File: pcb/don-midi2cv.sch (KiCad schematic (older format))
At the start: 17 parts

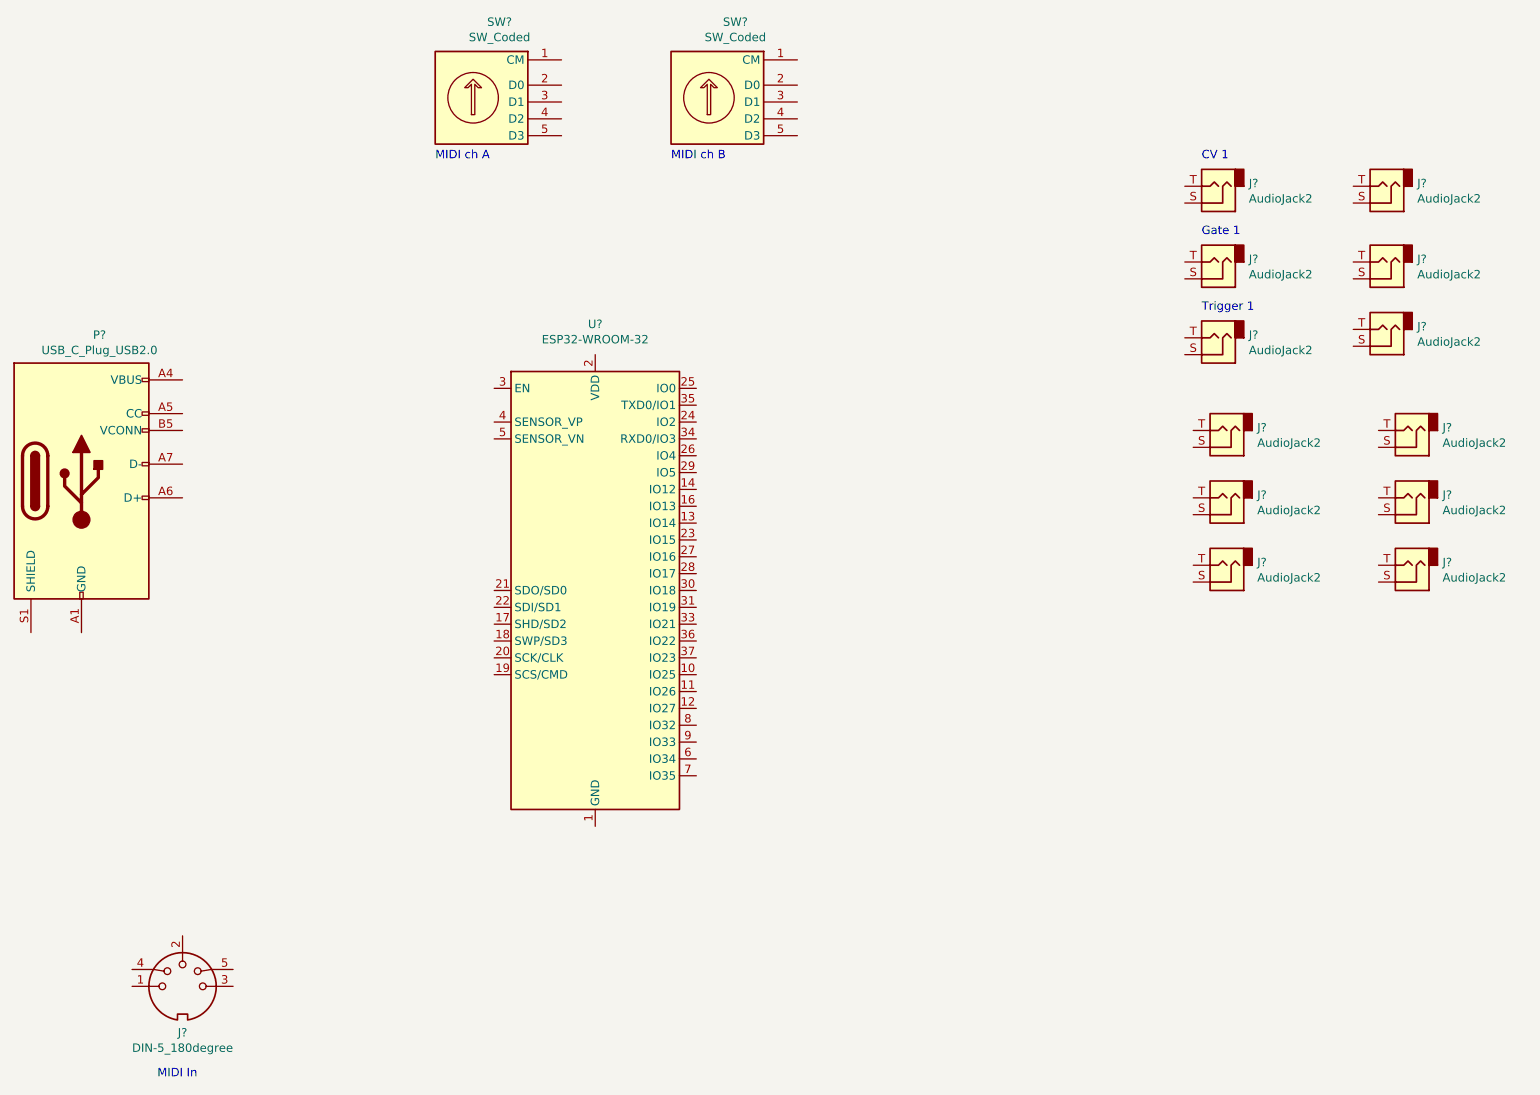
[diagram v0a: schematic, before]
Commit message: replace esp32 with stm32f103
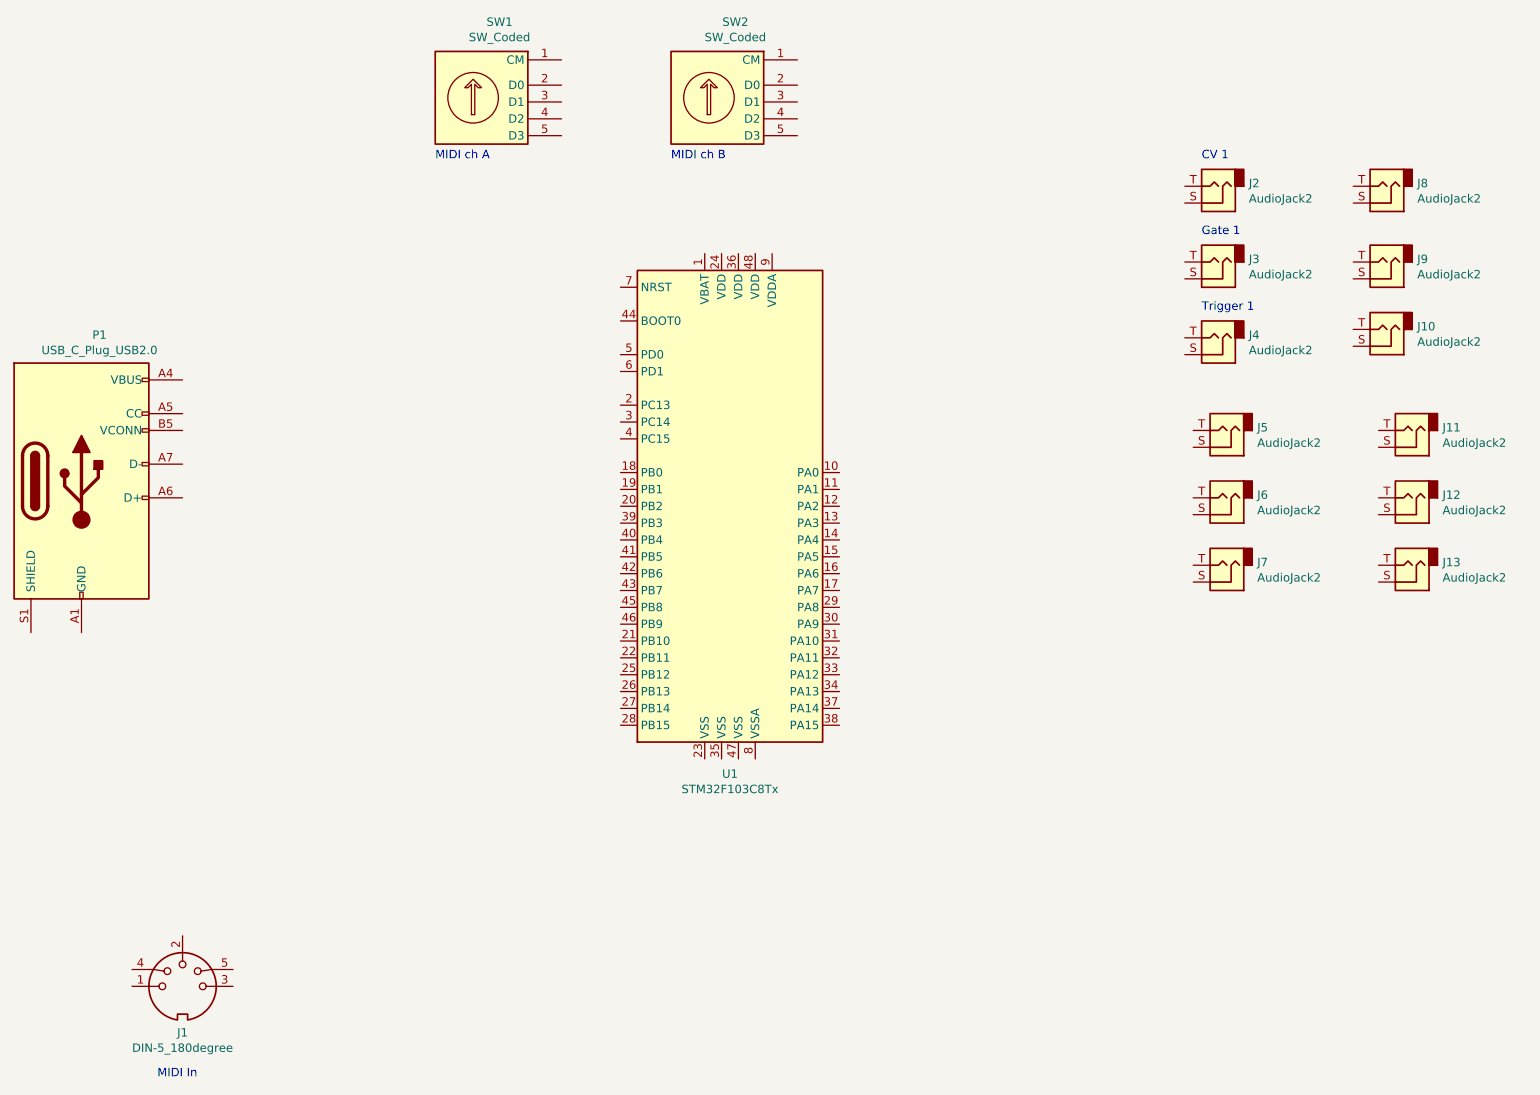
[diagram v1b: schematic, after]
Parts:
- removed U?: ESP32-WROOM-32, RF_Module:ESP32-WROOM-32, symbol RF_Module:ESP32-WROOM-32
- added U1: STM32F103C8Tx, Package_QFP:LQFP-48_7x7mm_P0.5mm, symbol MCU_ST_STM32F1:STM32F103C8Tx
- gave numbers to parts that had none: 16
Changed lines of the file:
@@
 $EndDescr
 $Comp
-L Connector:AudioJack2 J?
+L Connector:AudioJack2 J2
 U 1 1 5F82CE48
 P 8400 2000
-F 0 "J?" H 8220 1983 50  0000 R CNN
+F 0 "J2" H 8220 1983 50  0000 R CNN
 F 1 "AudioJack2" H 8220 2074 50  0000 R CNN
 F 2 "" H 8400 2000 50  0001 C CNN
@@
 CV 1
 $Comp
-L Connector:AudioJack2 J?
+L Connector:AudioJack2 J3
 U 1 1 5F82E376
 P 8400 2450
-F 0 "J?" H 8220 2433 50  0000 R CNN
+F 0 "J3" H 8220 2433 50  0000 R CNN
 F 1 "AudioJack2" H 8220 2524 50  0000 R CNN
 F 2 "" H 8400 2450 50  0001 C CNN
@@
 Gate 1
 $Comp
-L Connector:AudioJack2 J?
+L Connector:AudioJack2 J4
 U 1 1 5F82EBEA
 P 8400 2900
-F 0 "J?" H 8220 2883 50  0000 R CNN
+F 0 "J4" H 8220 2883 50  0000 R CNN
 F 1 "AudioJack2" H 8220 2974 50  0000 R CNN
 F 2 "" H 8400 2900 50  0001 C CNN
@@
 Trigger 1
 $Comp
-L Connector:USB_C_Plug_USB2.0 P?
+L Connector:USB_C_Plug_USB2.0 P1
 U 1 1 5F82F6C3
 P 1650 3750
-F 0 "P?" H 1757 4617 50  0000 C CNN
+F 0 "P1" H 1757 4617 50  0000 C CNN
 F 1 "USB_C_Plug_USB2.0" H 1757 4526 50  0000 C CNN
 F 2 "" H 1800 3750 50  0001 C CNN
@@
 $EndComp
 $Comp
-L RF_Module:ESP32-WROOM-32 U?
-U 1 1 5F837630
-P 4700 4400
-F 0 "U?" H 4700 5981 50  0000 C CNN
-F 1 "ESP32-WROOM-32" H 4700 5890 50  0000 C CNN
-F 2 "RF_Module:ESP32-WROOM-32" H 4700 2900 50  0001 C CNN
-F 3 "https://www.espressif.com/sites/default/files/documentation/esp32-wroom-32_datasheet_en.pdf" H 4400 4450 50  0001 C CNN
-	1    4700 4400
-	1    0    0    -1
-$EndComp
-$Comp
-L Switch:SW_Coded SW?
+L Switch:SW_Coded SW1
 U 1 1 5F83CB52
 P 4000 1500
-F 0 "SW?" H 4132 1975 50  0000 C CNN
+F 0 "SW1" H 4132 1975 50  0000 C CNN
 F 1 "SW_Coded" H 4132 1884 50  0000 C CNN
 F 2 "" H 3975 1525 50  0001 C CNN
@@
 $EndComp
 $Comp
-L Switch:SW_Coded SW?
+L Switch:SW_Coded SW2
 U 1 1 5F83E8DD
 P 5400 1500
-F 0 "SW?" H 5532 1975 50  0000 C CNN
+F 0 "SW2" H 5532 1975 50  0000 C CNN
 F 1 "SW_Coded" H 5532 1884 50  0000 C CNN
 F 2 "" H 5375 1525 50  0001 C CNN
@@
 MIDI ch B
 $Comp
-L Connector:DIN-5_180degree J?
+L Connector:DIN-5_180degree J1
 U 1 1 5F83F7CD
 P 2250 6750
-F 0 "J?" H 2250 6475 50  0000 C CNN
+F 0 "J1" H 2250 6475 50  0000 C CNN
 F 1 "DIN-5_180degree" H 2250 6384 50  0000 C CNN
 F 2 "" H 2250 6750 50  0001 C CNN
@@
 MIDI In
 $Comp
-L Connector:AudioJack2 J?
+L Connector:AudioJack2 J8
 U 1 1 5F847D1D
 P 9400 2000
-F 0 "J?" H 9220 1983 50  0000 R CNN
+F 0 "J8" H 9220 1983 50  0000 R CNN
 F 1 "AudioJack2" H 9220 2074 50  0000 R CNN
 F 2 "" H 9400 2000 50  0001 C CNN
@@
 $EndComp
 $Comp
-L Connector:AudioJack2 J?
+L Connector:AudioJack2 J9
 U 1 1 5F848051
 P 9400 2450
-F 0 "J?" H 9220 2433 50  0000 R CNN
+F 0 "J9" H 9220 2433 50  0000 R CNN
 F 1 "AudioJack2" H 9220 2524 50  0000 R CNN
 F 2 "" H 9400 2450 50  0001 C CNN
@@
 $EndComp
 $Comp
-L Connector:AudioJack2 J?
+L Connector:AudioJack2 J10
 U 1 1 5F848751
 P 9400 2850
-F 0 "J?" H 9220 2833 50  0000 R CNN
+F 0 "J10" H 9220 2833 50  0000 R CNN
 F 1 "AudioJack2" H 9220 2924 50  0000 R CNN
 F 2 "" H 9400 2850 50  0001 C CNN
@@
 $EndComp
 $Comp
-L Connector:AudioJack2 J?
+L Connector:AudioJack2 J5
 U 1 1 5F848F29
 P 8450 3450
-F 0 "J?" H 8270 3433 50  0000 R CNN
+F 0 "J5" H 8270 3433 50  0000 R CNN
 F 1 "AudioJack2" H 8270 3524 50  0000 R CNN
 F 2 "" H 8450 3450 50  0001 C CNN
@@
 $EndComp
 $Comp
-L Connector:AudioJack2 J?
+L Connector:AudioJack2 J6
 U 1 1 5F849500
 P 8450 3850
-F 0 "J?" H 8270 3833 50  0000 R CNN
+F 0 "J6" H 8270 3833 50  0000 R CNN
 F 1 "AudioJack2" H 8270 3924 50  0000 R CNN
 F 2 "" H 8450 3850 50  0001 C CNN
@@
 $EndComp
 $Comp
-L Connector:AudioJack2 J?
+L Connector:AudioJack2 J7
 U 1 1 5F849B5E
 P 8450 4250
-F 0 "J?" H 8270 4233 50  0000 R CNN
+F 0 "J7" H 8270 4233 50  0000 R CNN
 F 1 "AudioJack2" H 8270 4324 50  0000 R CNN
 F 2 "" H 8450 4250 50  0001 C CNN
@@
 $EndComp
 $Comp
-L Connector:AudioJack2 J?
+L Connector:AudioJack2 J11
 U 1 1 5F84A0C9
 P 9550 3450
-F 0 "J?" H 9370 3433 50  0000 R CNN
+F 0 "J11" H 9370 3433 50  0000 R CNN
 F 1 "AudioJack2" H 9370 3524 50  0000 R CNN
 F 2 "" H 9550 3450 50  0001 C CNN
@@
 $EndComp
 $Comp
-L Connector:AudioJack2 J?
+L Connector:AudioJack2 J12
 U 1 1 5F84A541
 P 9550 3850
-F 0 "J?" H 9370 3833 50  0000 R CNN
+F 0 "J12" H 9370 3833 50  0000 R CNN
 F 1 "AudioJack2" H 9370 3924 50  0000 R CNN
 F 2 "" H 9550 3850 50  0001 C CNN
@@
 $EndComp
 $Comp
-L Connector:AudioJack2 J?
+L Connector:AudioJack2 J13
 U 1 1 5F84AB69
 P 9550 4250
-F 0 "J?" H 9370 4233 50  0000 R CNN
+F 0 "J13" H 9370 4233 50  0000 R CNN
 F 1 "AudioJack2" H 9370 4324 50  0000 R CNN
 F 2 "" H 9550 4250 50  0001 C CNN
@@
 	-1   0    0    1
 $EndComp
+$Comp
+L MCU_ST_STM32F1:STM32F103C8Tx U1
+U 1 1 5F83956E
+P 5550 3900
+F 0 "U1" H 5500 2311 50  0000 C CNN
+F 1 "STM32F103C8Tx" H 5500 2220 50  0000 C CNN
+F 2 "Package_QFP:LQFP-48_7x7mm_P0.5mm" H 4950 2500 50  0001 R CNN
+F 3 "http://www.st.com/st-web-ui/static/active/en/resource/technical/document/datasheet/CD00161566.pdf" H 5550 3900 50  0001 C CNN
+	1    5550 3900
+	1    0    0    -1
+$EndComp
 $EndSCHEMATC
